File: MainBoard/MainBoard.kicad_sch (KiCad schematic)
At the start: 55 parts, among them IC1 BQ25171QWDRCRQ1, J1 KH-TYPE-C-16P, U1 STM32L496VGY6PTR, U2 MX25R1635FZUIL0, U3 SI3477DV-T1-GE3, U4 SI3477DV-T1-GE3, U5 TPS63802DLAR, U6 FUSB302BMPX, U7 BNO086, Y1 9HT11-32.768KBZF-T

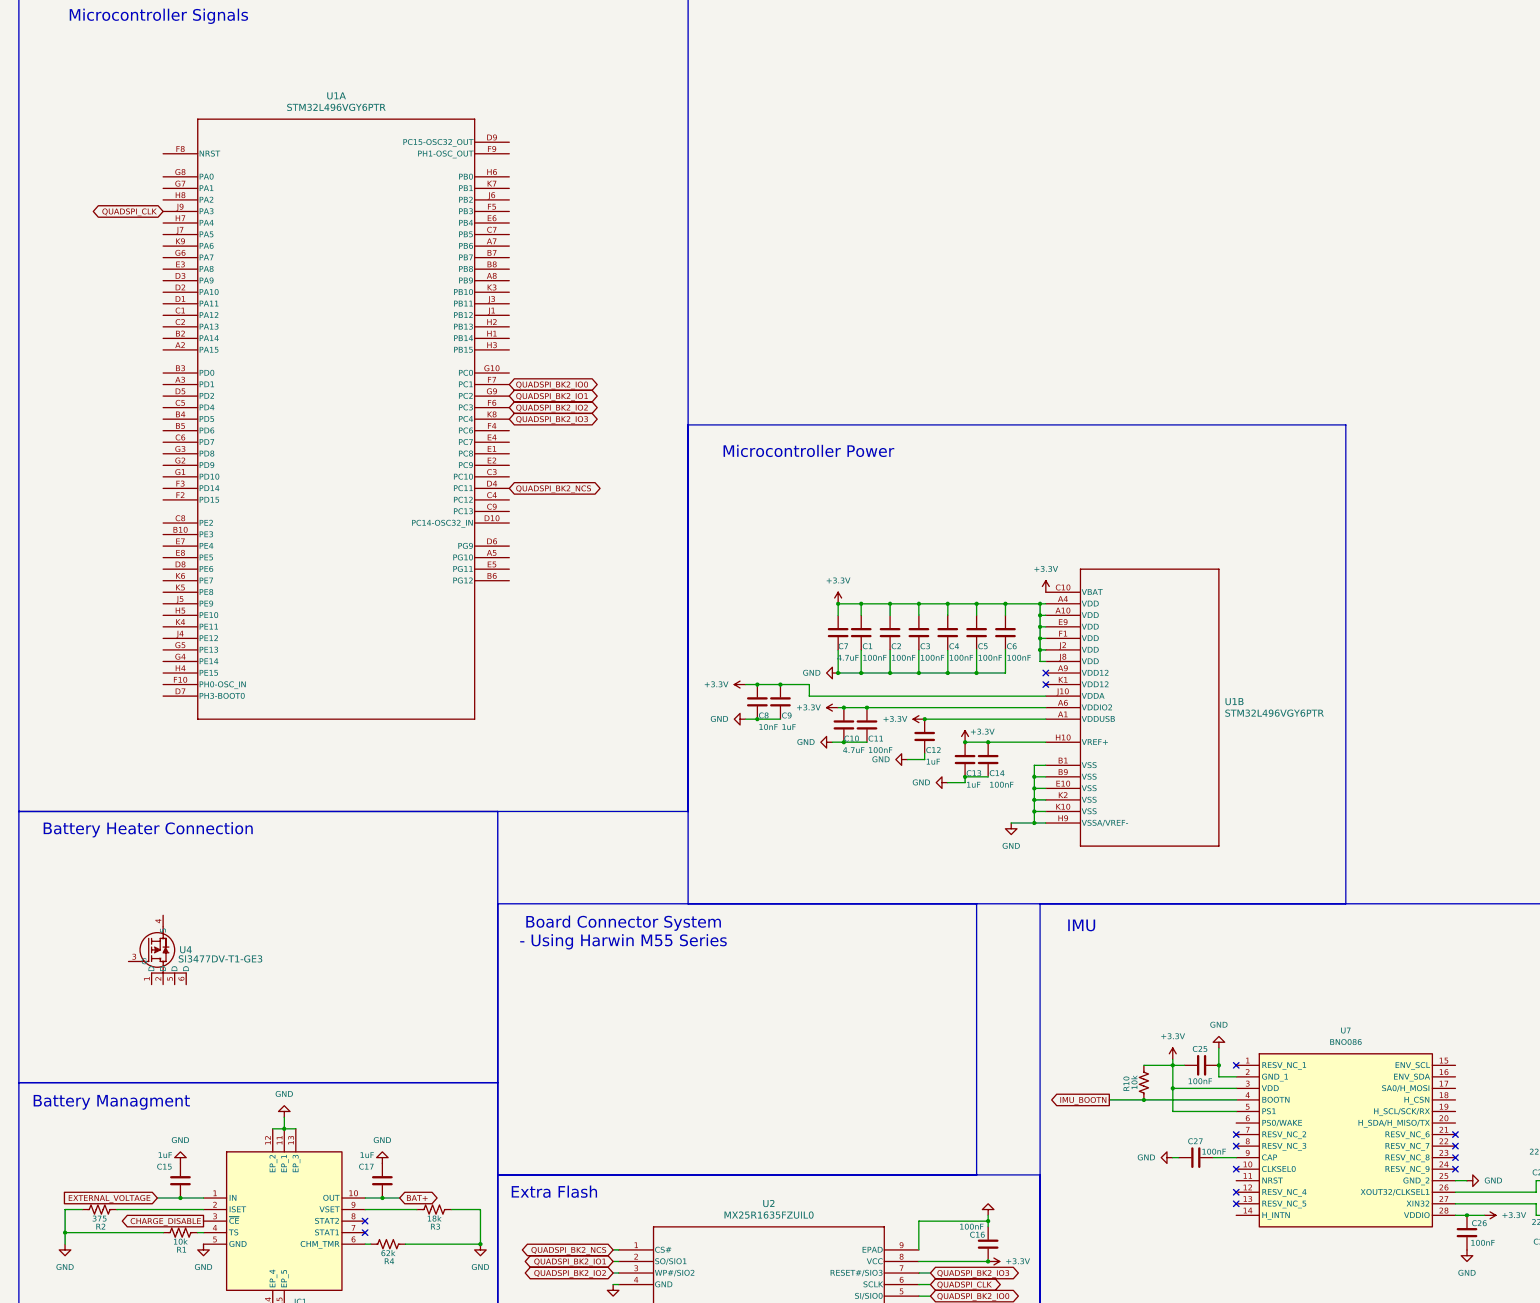
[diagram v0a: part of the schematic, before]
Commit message: yoshita worked on IMU pins, about half done with connecting the pins
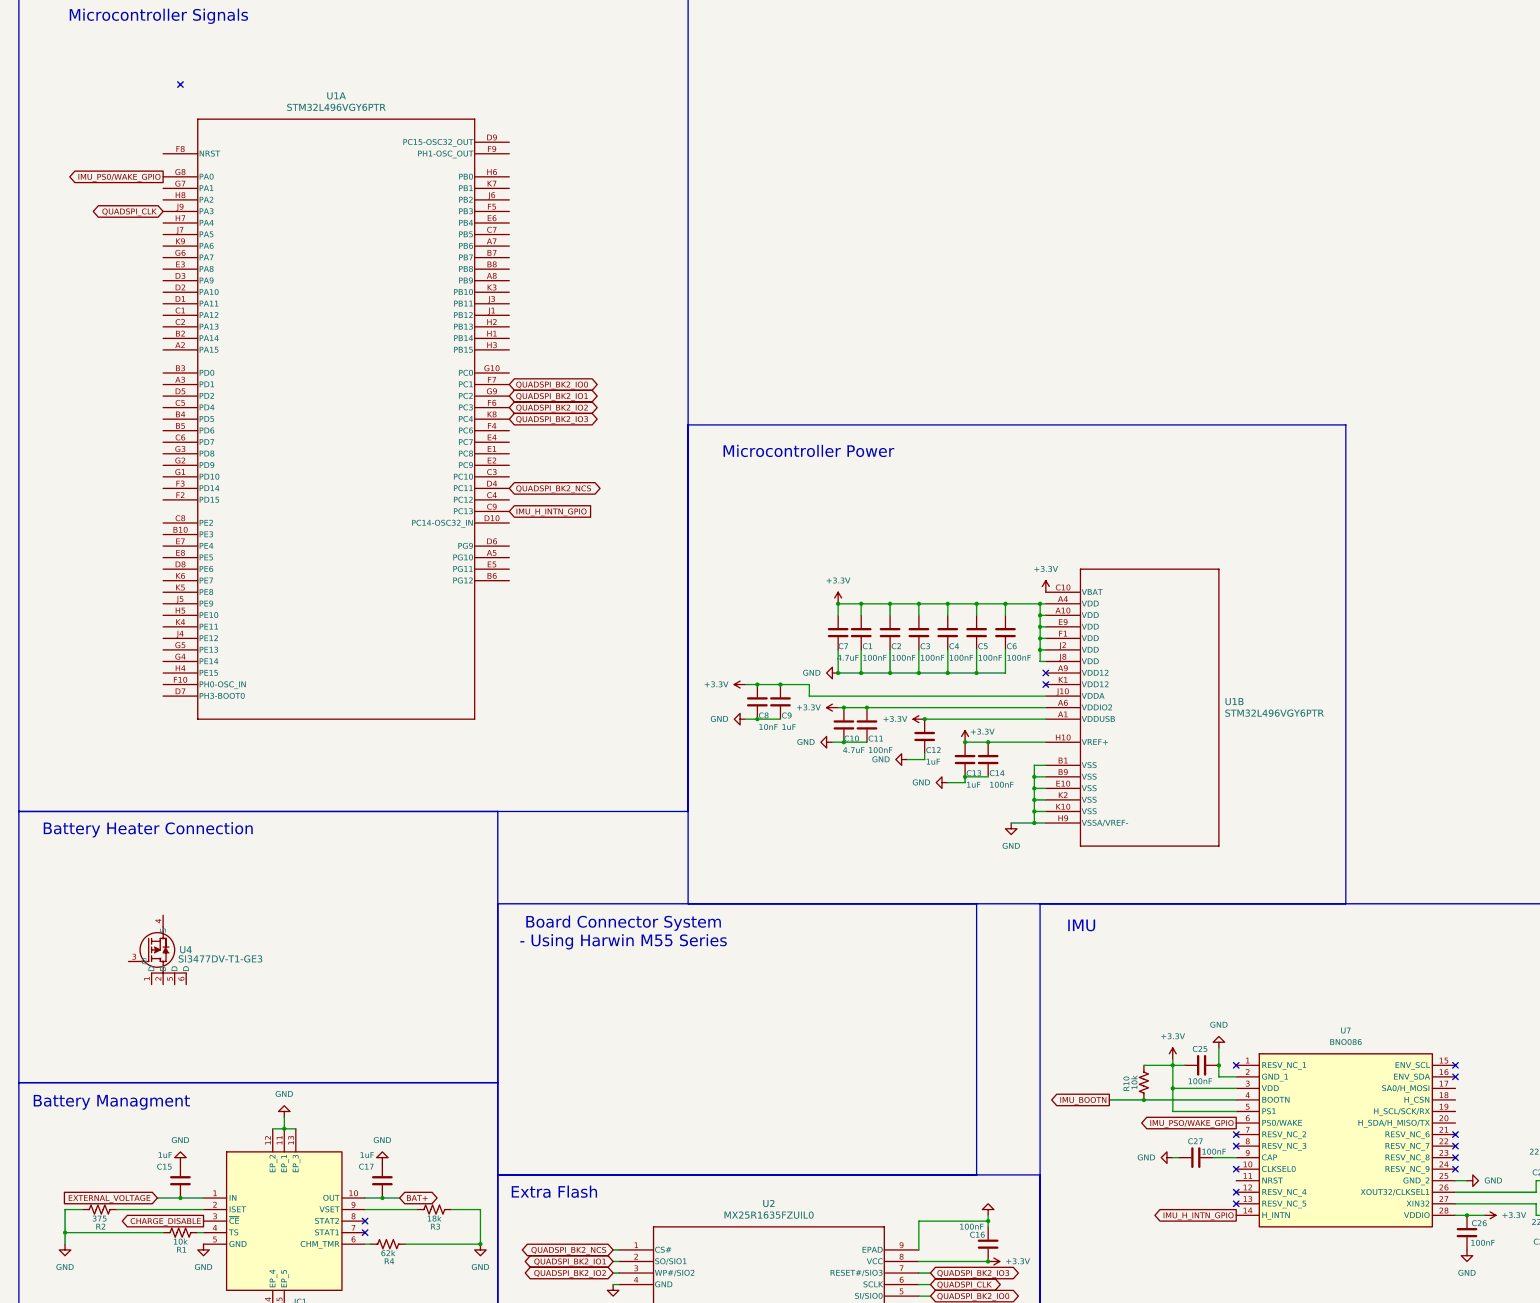
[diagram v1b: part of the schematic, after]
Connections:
- net IMU_H_INTN_GPIO: now reaches U1.C9 (PC13)
- net IMU_H_INTN_GPIO: now also U7.14 (H_INTN)
- net IMU_PS0/WAKE_GPIO: now reaches U1.G8 (PA0)
- net IMU_PSO/WAKE_GPIO: now reaches U7.6 (PS0/WAKE)
- no-connect marks 28 -> 31
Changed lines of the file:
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@@
+	)
+	(no_connect
+		(at 45.72 73.66)
 	)
 	(no_connect
@@
 	)
 	(no_connect
+		(at 326.39 292.1)
+	)
+	(no_connect
 		(at 156.21 374.65)
 	)
@@
 	)
 	(no_connect
+		(at 326.39 289.56)
+	)
+	(no_connect
 		(at 278.13 307.34)
 	)
@@
 			(width 0)
 			(type default)
+		)
+	)
+	(global_label "IMU_PS0{slash}WAKE_GPIO"
+		(shape output)
+		(at 41.91 93.98 180)
+		(fields_autoplaced yes)
+		(effects
+			(font
+				(size 1.27 1.27)
+			)
+			(justify right)
+		)
+		(property "Intersheetrefs" "${INTERSHEET_REFS}"
+			(at 19.1491 93.98 0)
+			(effects
+				(font
+					(size 1.27 1.27)
+				)
+				(justify right)
+				(hide yes)
+			)
 		)
 	)
@@
 		)
 	)
+	(global_label "IMU_PSO{slash}WAKE_GPIO"
+		(shape output)
+		(at 278.13 302.26 180)
+		(fields_autoplaced yes)
+		(effects
+			(font
+				(size 1.27 1.27)
+			)
+			(justify right)
+		)
+		(property "Intersheetrefs" "${INTERSHEET_REFS}"
+			(at 255.2481 302.26 0)
+			(effects
+				(font
+					(size 1.27 1.27)
+				)
+				(justify right)
+				(hide yes)
+			)
+		)
+	)
 	(global_label "BAT+"
 		(shape bidirectional)
@@
 		)
 	)
+	(global_label "IMU_H_INTN_GPIO"
+		(shape output)
+		(at 278.13 322.58 180)
+		(fields_autoplaced yes)
+		(effects
+			(font
+				(size 1.27 1.27)
+			)
+			(justify right)
+		)
+		(property "Intersheetrefs" "${INTERSHEET_REFS}"
+			(at 258.8161 322.58 0)
+			(effects
+				(font
+					(size 1.27 1.27)
+				)
+				(justify right)
+				(hide yes)
+			)
+		)
+	)
 	(global_label "QUADSPI_BK2_IO2"
 		(shape bidirectional)
@@
 			(effects
 				(font
+					(size 1.27 1.27)
+				)
+				(justify left)
+				(hide yes)
+			)
+		)
+	)
+	(global_label "IMU_H_INTN_GPIO"
+		(shape input)
+		(at 118.11 167.64 0)
+		(fields_autoplaced yes)
+		(effects
+			(font
+				(size 1.27 1.27)
+			)
+			(justify left)
+		)
+		(property "Intersheetrefs" "${INTERSHEET_REFS}"
+			(at 137.4239 167.64 0)
+			(effects
+				(font

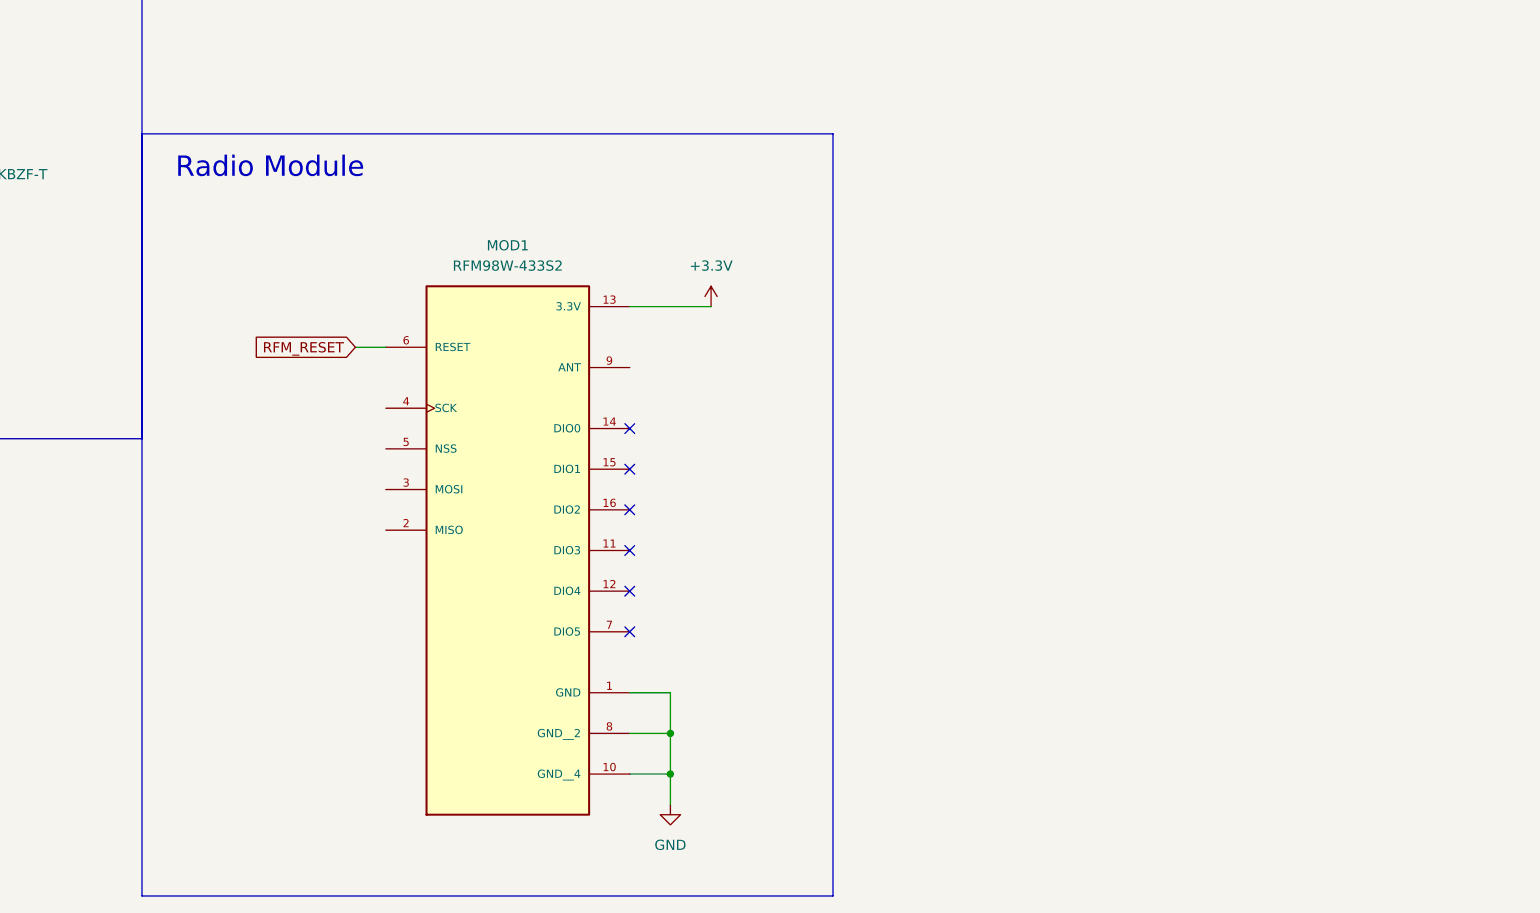
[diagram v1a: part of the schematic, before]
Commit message: Add CAN transceiver - removed radio module
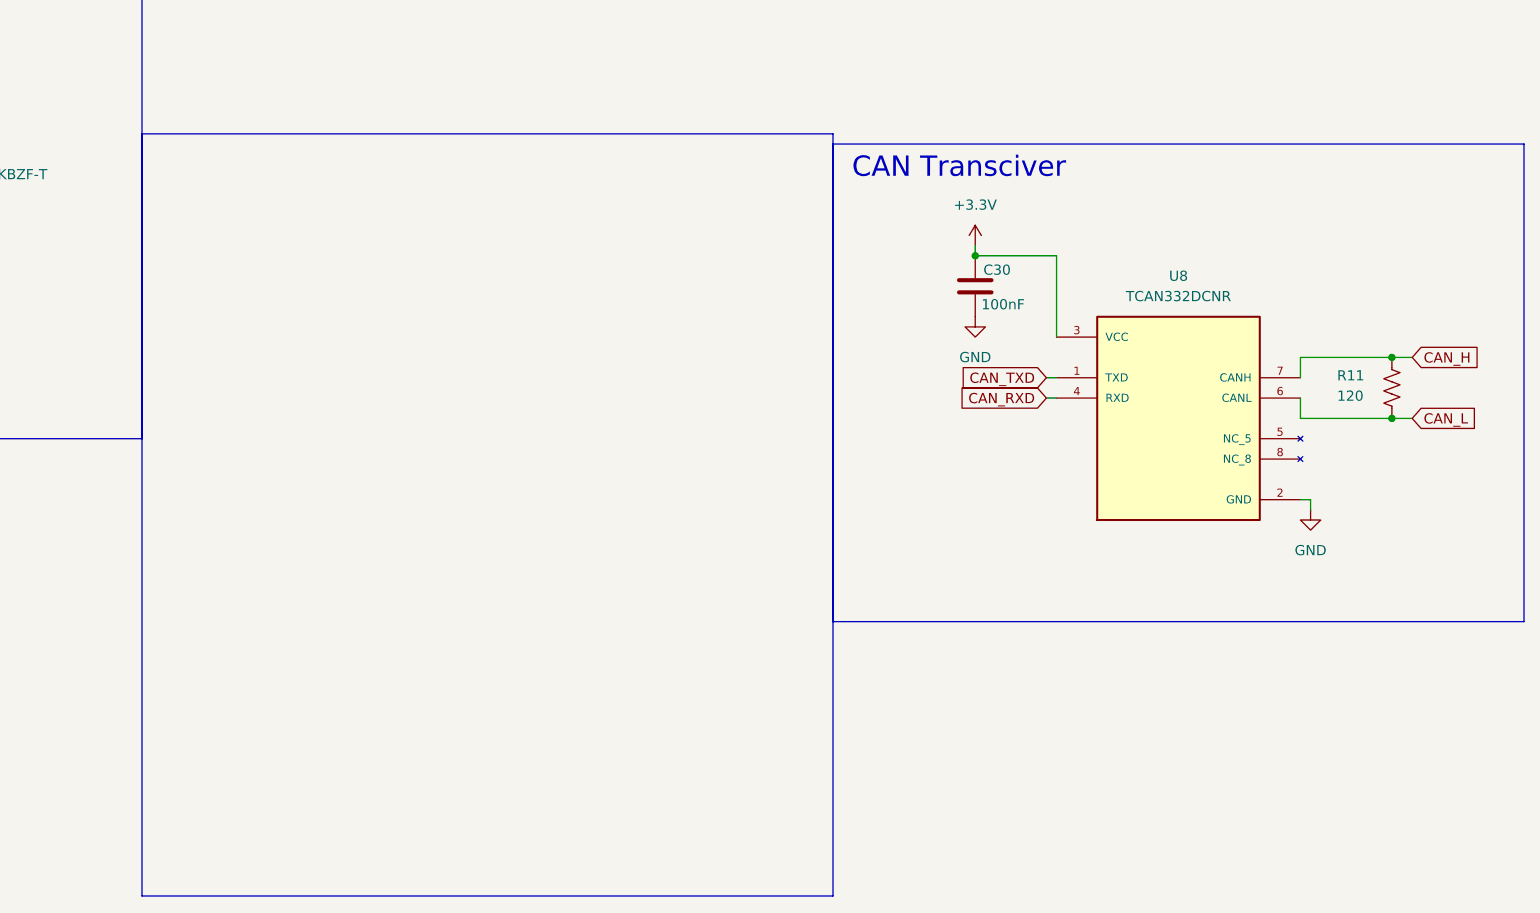
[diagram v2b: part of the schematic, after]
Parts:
- removed MOD1: RFM98W-433S2, inspirefly:XCVR_RFM98W-433S2, symbol inspirefly:RFM98W-433S2
- added C30: 100nF, Capacitor_SMD:C_0402_1005Metric_Pad0.74x0.62mm_HandSolder, symbol Device:C
- added R11: 120, Resistor_SMD:R_0402_1005Metric_Pad0.72x0.64mm_HandSolder, symbol Device:R_US
- added U8: TCAN332DCNR, inspirefly:SOT65P280X145-8N, symbol inspirefly:TCAN332DCNR
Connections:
- net +3.3V: now also C30.1, U8.3 (VCC)
- net GND: now also C30.2, U8.2 (GND)
- new net CAN_H: R11.2, U8.7 (CANH)
- new net CAN_L: R11.1, U8.6 (CANL)
- new net CAN_RXD: U8.4 (RXD)
- new net CAN_TXD: U8.1 (TXD)
- no-connect marks 31 -> 25
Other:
- note added: "CAN Transciver"
- note removed: "Radio Module"

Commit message: Integrated BQ25756E along with schematic changes
Removed old Battery management, replaced with BQ25756E. Schematic work complete along with external part finding.
Dedicated section to I2C pull ups.
Moved around items in schematics for better look.
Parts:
- removed C15, C17: 1uF, Capacitor_SMD:C_0402_1005Metric_Pad0.74x0.62mm_HandSolder, symbol Device:C
- removed IC1: BQ25171QWDRCRQ1, inspirefly:BQ25171QWDRCRQ1, symbol inspirefly:BQ25171QWDRCRQ1
- added C28, C29, C34, C35, C39, C40, C46, C47: 22uF, Capacitor_SMD:C_0402_1005Metric_Pad0.74x0.62mm_HandSolder, symbol Device:C
- added C30, C32, C41, C42, C43, C45: 100nF, Capacitor_SMD:C_0402_1005Metric_Pad0.74x0.62mm_HandSolder, symbol Device:C
- added C31, C44: 470nF, Capacitor_SMD:C_0402_1005Metric_Pad0.74x0.62mm_HandSolder, symbol Device:C
- added C36, C37: 4.7uF, Capacitor_SMD:C_0402_1005Metric_Pad0.74x0.62mm_HandSolder, symbol Device:C
- added C38: 1uF, Capacitor_SMD:C_0402_1005Metric_Pad0.74x0.62mm_HandSolder, symbol Device:C
- added D2: LED, LED_SMD:LED_0402_1005Metric, symbol Device:LED
- added L2: 4.7uH, inspirefly:WE-LQSA_5040, symbol Device:L
- added Q1, Q2, Q3, Q4: PMV19XNEAR, inspirefly:TO-236AB_SOT23_NEX, symbol inspirefly:PMV19XNEAR
- added R14: 143k, Resistor_SMD:R_0402_1005Metric_Pad0.72x0.64mm_HandSolder, symbol Device:R_US
- added R15, R22: 250k, Resistor_SMD:R_0402_1005Metric_Pad0.72x0.64mm_HandSolder, symbol Device:R_US
- added R16: 6.2k, Resistor_SMD:R_0402_1005Metric_Pad0.72x0.64mm_HandSolder, symbol Device:R_US
- added R17: 36k, Resistor_SMD:R_0402_1005Metric_Pad0.72x0.64mm_HandSolder, symbol Device:R_US
- added R18, R23, R27, R28, R30: 10, Resistor_SMD:R_0402_1005Metric_Pad0.72x0.64mm_HandSolder, symbol Device:R_US
- added R19: 25k, Resistor_SMD:R_0402_1005Metric_Pad0.72x0.64mm_HandSolder, symbol Device:R_US
- added R20: 40k, Resistor_SMD:R_0402_1005Metric_Pad0.72x0.64mm_HandSolder, symbol Device:R_US
- added R21, R29: 5m, Resistor_SMD:R_1206_3216Metric_Pad1.30x1.75mm_HandSolder, symbol Device:R_US
- added R24, R26: 10k, Resistor_SMD:R_0402_1005Metric_Pad0.72x0.64mm_HandSolder, symbol Device:R_US
- added R5, R6, R7: 2.2k, Resistor_SMD:R_0402_1005Metric_Pad0.72x0.64mm_HandSolder, symbol Device:R_US
- added U8: BQ25756ERRVR, inspirefly:IC_BQ25756ERRVR, symbol inspirefly:BQ25756ERRVR
- R1: value 10k -> 2.2k
- R2: value 375 -> 2.2k
- R3: value 18k -> 2.2k
- R4: value 62k -> 2.2k
- R8, R9: value 4.7k -> 2.2k
- renumbered C21 to C1, C7 to C10, C10 to C11, C1 to C12, C11 to C13, C2 to C14, C3 to C15, C12 to C16, C4 to C17, C13 to C19, C22 to C2, C5 to C20, C14 to C21, C26 to C22, C6 to C23, C28 to C24, C29 to C25, C20 to C26, C19 to C27, C16 to C3, C30 to C33, C27 to C4, C25 to C5, C23 to C6, C24 to C7, R6 to R11, R7 to R12, R5 to R13, R11 to R25, U2 to U1, U4 to U2, U1 to U3, U6 to U4, U7 to U5, U5 to U6, U3 to U7, U8 to U9
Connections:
- net +3.3V: now also R1.1, R2.2, R3.1, R4.2, R8.2, R9.2, R24.2, R5.1, R6.2, R7.1
- net BAT+: now also C46.1, C47.1, R15.2, R29.2, R30.2
- net EXTERNAL_VOLTAGE: now also C28.1, C29.1, C38.2, R18.2, R21.1, U8.32 (VAC), U8.33 (VAC__1), U8.34 (ACUV)
- net GND: now also C28.2, C29.2, C30.2, C32.1, C34.2, C35.2, C36.2, C37.2, C38.1, C39.2, C40.2, C41.2, C42.1, C43.2, C45.1, C46.2, C47.2, Q2.2 (S), Q4.2 (S), R17.2, R19.2, R20.1, R22.2, U8.17 (PGND), U8.22 (PGND__1), U8.35 (ACOV), U8.37 (PGND__2), U8.7 (~{CE}); no longer R1.1, R2.1, R3.2, R4.2, R8.2, R9.1
- net I2C1_SCL: now also R2.1; no longer R8.1
- net I2C1_SDA: now also R1.2; no longer R9.2
- net I2C2_SCL: now reaches R4.1
- net I2C2_SCL: now also U8.1 (SCL)
- net INT_N: now reaches U4.5 (INT_N)
- net INT_N: now also R8.1
- new net: D2.1 (K), R26.1
- new net: C39.1, C40.1, Q3.3 (D), R28.2, R29.1
- new net: C34.1, C35.1, Q1.3 (D), R21.2, R23.2
- new net: R19.1, U8.9 (ICHG)
- new net: R22.1, U8.10 (ILIM_HIZ)
- new net: R14.1, U8.11 (FBG)
- new net: R14.2, R15.1, U8.12 (FB)
- new net: C36.1, R27.1, U8.23 (DRV_SUP)
- new net: R20.2, U8.36 (FSW_SYNC)
- new net: R26.2, U8.6 (~{PG})
- new net ACN: C31.2, C32.2, R23.1, U8.29 (ACN)
- new net ACP: C30.1, C31.1, R18.1, U8.30 (ACP)
- new net BAT_HIGH_SIDE_DRIVE: Q3.1 (G), U8.19 (HIDRV2)
- new net BAT_LOW_SIDE_DRIVE: Q4.1 (G), U8.21 (LODRV2)
- new net BAT_SIDE_INDUC: C42.2, L2.2, Q3.2 (S), Q4.3 (D), U8.18 (SW2), U8.20 (BTST2)
- new net BQ_INT_DIN: R24.1, U8.3 (~{INT})
- new net EXTERNAL_HIGH_SIDE_DRIVE: Q1.1 (G), U8.27 (HIDRV1)
- new net EXTERNAL_LOW_SIDE_DRIVE: Q2.1 (G), U8.25 (LODRV1)
- new net EXTERNAL_SIDE_INDUC: C41.1, L2.1, Q1.2 (S), Q2.3 (D), U8.26 (BTST1), U8.28 (SW1)
- new net I2C2_SDA: R3.2, U8.2 (SDA)
- new net I2C3_SCL: R6.1, R9.1
- new net I2C3_SDA: R5.2, R7.2
- new net REGN: C37.1, D2.2 (A), R16.1, R27.2, U8.24 (REGN)
- new net SRN: C44.2, C45.2, R30.1, U8.13 (SRN)
- new net SRP: C43.1, C44.1, R28.1, U8.14 (SRP)
- new net THERMISTOR_FEEDBACK: R16.2, R17.1, U8.8 (TS)
- no-connect marks 25 -> 23
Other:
- note added: "I2C Pullups"
- note added: "Wurth 78404054047"
- moved on the sheet: C18, C22, C24, C25, C26, C27, C3, C33, C4, C5, L1, R10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

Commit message: Changed bulk cap values
Removed parallel 22uF 0402 for bulks on battery management. Replaced with 47uF 1206 due to over voltage issues.
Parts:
- removed C28, C29, C46, C47: 22uF, Capacitor_SMD:C_0402_1005Metric_Pad0.74x0.62mm_HandSolder, symbol Device:C
- removed C3: 100nF, Capacitor_SMD:C_0402_1005Metric_Pad0.74x0.62mm_HandSolder, symbol Device:C
- removed U1: MX25R1635FZUIL0, inspirefly:USON-8L-2X3X0P6_MAC, symbol inspirefly:MX25R1635FZUIL0
- C34, C35, C39, C40: value 22uF -> 47uF; footprint Capacitor_SMD:C_0402_1005Metric_Pad0.74x0.62mm_HandSolder -> Capacitor_SMD:C_1206_3216Metric_Pad1.33x1.80mm_HandSolder
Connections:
- net BAT+: now also C39.1
- net EXTERNAL_VOLTAGE: now also C40.1
- net at Q3.3 (D), R28.2, R29.1: now also C34.1; no longer C39.1, C40.1
- net at C35.1, Q1.3 (D), R21.2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: no longer C34.1
- net QUADSPI_BK2_IO0: no longer names the net of U3.F7 (PC1)
- net QUADSPI_BK2_IO1: no longer names the net of U3.G9 (PC2)
- net QUADSPI_BK2_IO2: no longer names the net of U3.F6 (PC3)
- net QUADSPI_BK2_IO3: no longer names the net of U3.K8 (PC4)
- net QUADSPI_BK2_NCS: no longer names the net of U3.D4 (PC11)
- net QUADSPI_CLK: no longer names the net of U3.J9 (PA3)
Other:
- note removed: "Extra Flash"
